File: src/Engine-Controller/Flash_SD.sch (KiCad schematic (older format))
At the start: 5 parts, among them P6 Micro_SD_Card, U5 SST25VF040B-50-4I-S2AE-T

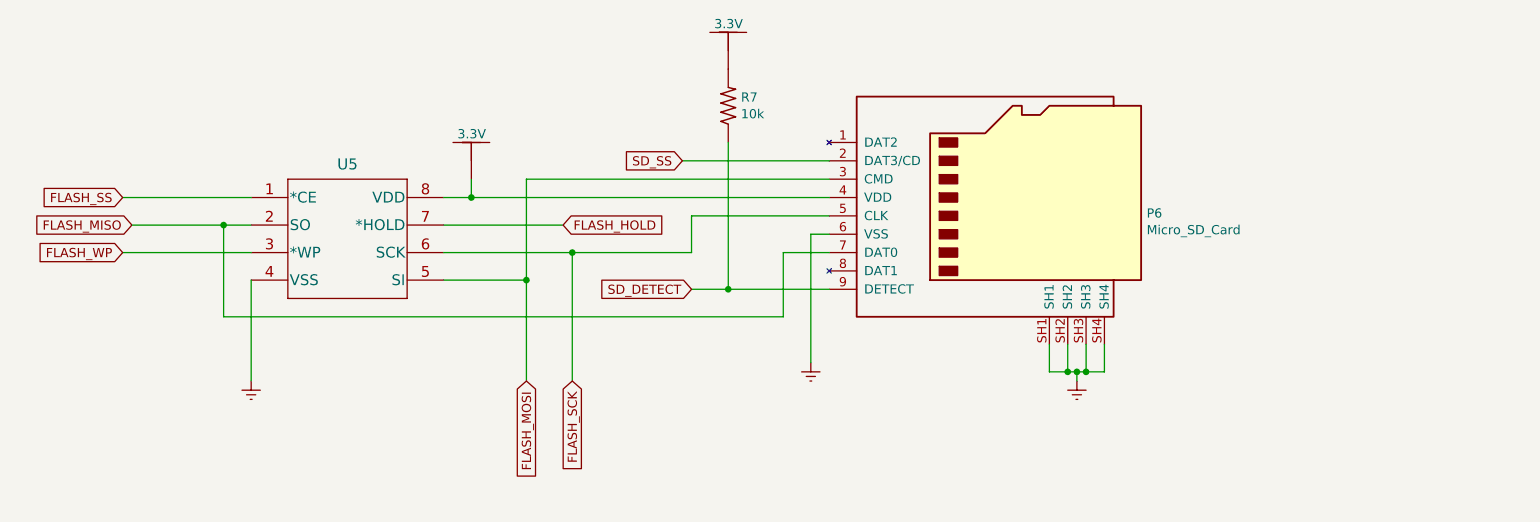
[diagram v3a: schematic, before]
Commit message: Added ADC Inputs
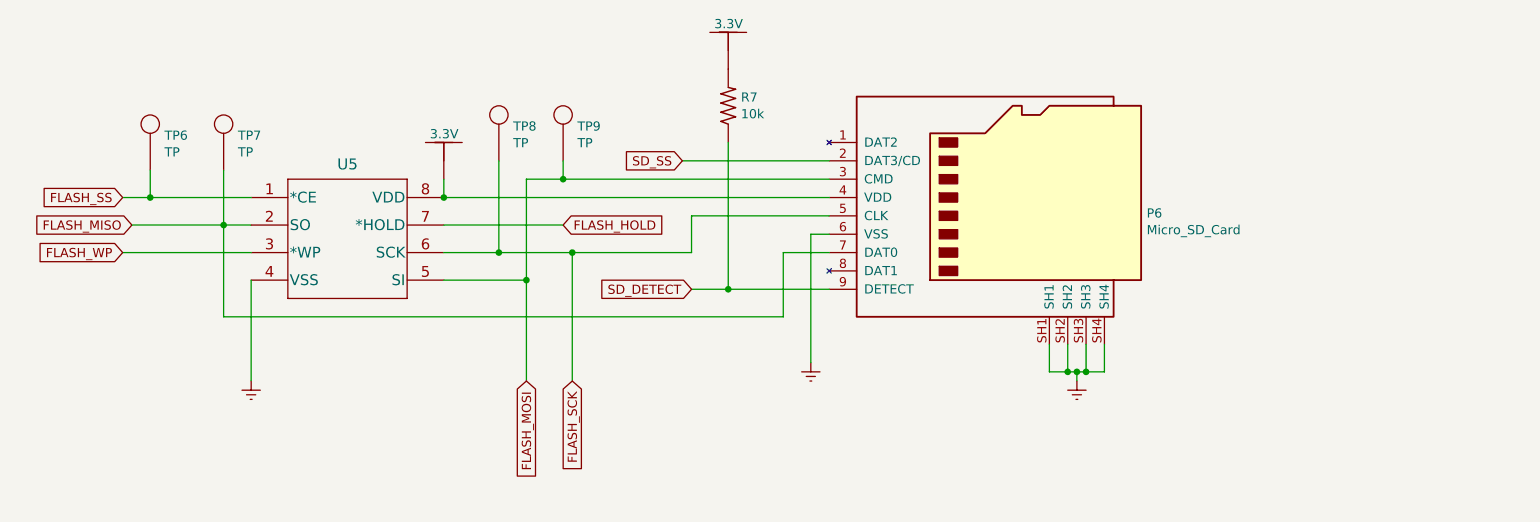
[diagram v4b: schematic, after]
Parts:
- added TP6, TP7, TP8, TP9: TP, symbol Engine-Controller:TP
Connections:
- net FLASH_MISO: now also TP7.1
- net FLASH_MOSI: now also TP9.1
- net FLASH_SCK: now also TP8.1
- net FLASH_SS: now also TP6.1
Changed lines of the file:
@@
 $Descr A4 11693 8268
 encoding utf-8
-Sheet 6 5
+Sheet 5 5
 Title "Data Logging Memory"
 Date "2021-07-03"
@@
 FLASH_SS
 Wire Wire Line
-	3300 3800 4000 3800
+	3300 3800 3450 3800
 Text GLabel 3350 3950 0    50   Input ~ 0
 FLASH_MISO
@@
 L Engine-Controller:3.3V None05
 U 1 1 617870C5
-P 5200 3550
-F 0 "None05" H 5328 3539 50  0001 L CNN
-F 1 "3.3V" H 5124 3646 50  0000 L CNN
-F 2 "" H 5200 3550 50  0001 C CNN
-F 3 "" H 5200 3550 50  0001 C CNN
-	1    5200 3550
-	1    0    0    -1
-$EndComp
-Wire Wire Line
-	5050 3800 5200 3800
-Wire Wire Line
-	5200 3800 5200 3700
+P 5050 3550
+F 0 "None05" H 5178 3539 50  0001 L CNN
+F 1 "3.3V" H 4974 3646 50  0000 L CNN
+F 2 "" H 5050 3550 50  0001 C CNN
+F 3 "" H 5050 3550 50  0001 C CNN
+	1    5050 3550
+	1    0    0    -1
+$EndComp
+Wire Wire Line
+	5050 3800 5050 3700
 $Comp
 L power:Earth #PWR03
@@
 FLASH_SCK
 Wire Wire Line
-	5750 4100 5050 4100
+	5750 4100 5350 4100
 Text GLabel 5500 4800 3    50   Input ~ 0
 FLASH_MOSI
@@
 	8650 4750 8550 4750
 Connection ~ 8550 4750
-Wire Wire Line
-	5200 3800 7150 3800
-Connection ~ 5200 3800
 Text GLabel 6350 3600 0    50   Input ~ 0
 SD_SS
@@
 	5500 4250 5500 3700
 Wire Wire Line
-	5500 3700 7150 3700
+	5500 3700 5700 3700
 Connection ~ 5500 4250
 Wire Wire Line
@@
 	1    0    0    -1
 $EndComp
+$Comp
+L Engine-Controller:TP TP6
+U 1 1 619D48B0
+P 3450 3650
+F 0 "TP6" H 3528 3838 50  0000 L CNN
+F 1 "TP" H 3528 3747 50  0000 L CNN
+F 2 "" H 3450 3650 50  0001 C CNN
+F 3 "" H 3450 3650 50  0001 C CNN
+	1    3450 3650
+	1    0    0    -1
+$EndComp
+$Comp
+L Engine-Controller:TP TP7
+U 1 1 619D6A4E
+P 3850 3650
+F 0 "TP7" H 3928 3838 50  0000 L CNN
+F 1 "TP" H 3928 3747 50  0000 L CNN
+F 2 "" H 3850 3650 50  0001 C CNN
+F 3 "" H 3850 3650 50  0001 C CNN
+	1    3850 3650
+	1    0    0    -1
+$EndComp
+$Comp
+L Engine-Controller:TP TP8
+U 1 1 619D874E
+P 5350 3600
+F 0 "TP8" H 5428 3788 50  0000 L CNN
+F 1 "TP" H 5428 3697 50  0000 L CNN
+F 2 "" H 5350 3600 50  0001 C CNN
+F 3 "" H 5350 3600 50  0001 C CNN
+	1    5350 3600
+	1    0    0    -1
+$EndComp
+Connection ~ 5050 3800
+Wire Wire Line
+	5050 3800 7150 3800
+$Comp
+L Engine-Controller:TP TP9
+U 1 1 619DE8D4
+P 5700 3600
+F 0 "TP9" H 5778 3788 50  0000 L CNN
+F 1 "TP" H 5778 3697 50  0000 L CNN
+F 2 "" H 5700 3600 50  0001 C CNN
+F 3 "" H 5700 3600 50  0001 C CNN
+	1    5700 3600
+	1    0    0    -1
+$EndComp
+Wire Wire Line
+	3450 3650 3450 3800
+Connection ~ 3450 3800
+Wire Wire Line
+	3450 3800 4000 3800
+Wire Wire Line
+	3850 3650 3850 3950
+Wire Wire Line
+	5350 3600 5350 4100
+Connection ~ 5350 4100
+Wire Wire Line
+	5350 4100 5050 4100
+Wire Wire Line
+	5700 3600 5700 3700
+Connection ~ 5700 3700
+Wire Wire Line
+	5700 3700 7150 3700
 $EndSCHEMATC

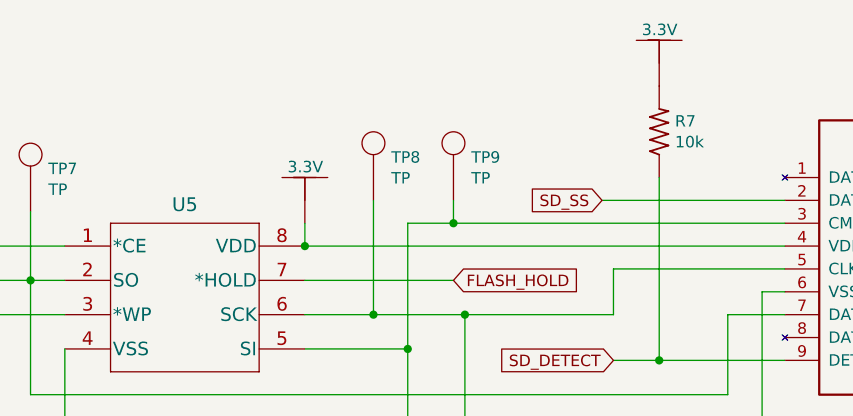
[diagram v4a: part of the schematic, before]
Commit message: Fixed Schematic ERC erros
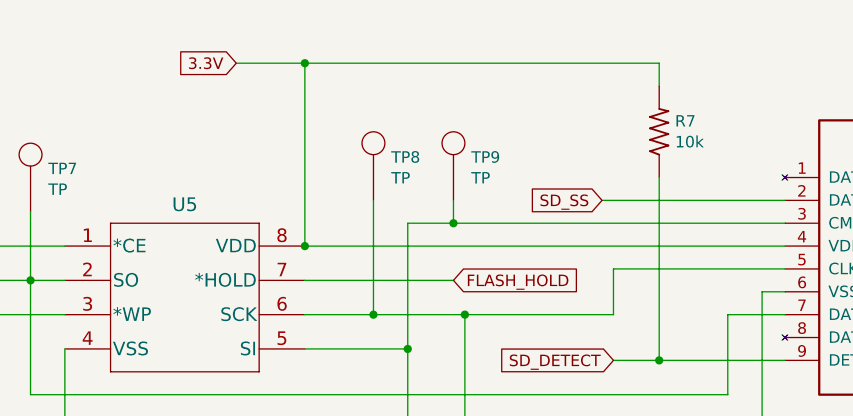
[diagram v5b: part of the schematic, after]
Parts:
- removed None05, None06: 3.3V, symbol Engine-Controller:3.3V
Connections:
- net 3.3V: now reaches P6.4 (VDD), U5.8 (VDD)
- net 3.3V: now also R7.2
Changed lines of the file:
@@
 	4000 4100 3300 4100
-$Comp
-L Engine-Controller:3.3V None05
-U 1 1 617870C5
-P 5050 3550
-F 0 "None05" H 5178 3539 50  0001 L CNN
-F 1 "3.3V" H 4974 3646 50  0000 L CNN
-F 2 "" H 5050 3550 50  0001 C CNN
-F 3 "" H 5050 3550 50  0001 C CNN
-	1    5050 3550
-	1    0    0    -1
-$EndComp
-Wire Wire Line
-	5050 3800 5050 3700
 $Comp
 L power:Earth #PWR03
@@
 	6600 4300 6400 4300
 $Comp
-L Engine-Controller:3.3V None06
-U 1 1 618DC655
-P 6600 2950
-F 0 "None06" H 6728 2939 50  0001 L CNN
-F 1 "3.3V" H 6524 3046 50  0000 L CNN
-F 2 "" H 6600 2950 50  0001 C CNN
-F 3 "" H 6600 2950 50  0001 C CNN
-	1    6600 2950
-	1    0    0    -1
-$EndComp
-$Comp
 L Engine-Controller:TP TP6
 U 1 1 619D48B0
@@
 Wire Wire Line
 	5700 3700 7150 3700
+Text GLabel 4750 3000 0    50   Input ~ 0
+3.3V
+Wire Wire Line
+	4750 3000 5050 3000
+Wire Wire Line
+	6600 3000 6600 3100
+Wire Wire Line
+	5050 3000 5050 3800
+Connection ~ 5050 3000
+Wire Wire Line
+	5050 3000 6600 3000
 $EndSCHEMATC

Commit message: Routed decoupling caps
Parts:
- P6: footprint (none) -> Engine-Controller:GCT_MEM2075-00-140-01-A
- R7: footprint (none) -> Engine-Controller:RES_0603
- TP6, TP7, TP8, TP9: footprint (none) -> Engine-Controller:TP
- U5: footprint SOIC8_S2A_SST_MCH -> Engine-Controller:SST25VF040B-50-4I-S2AE-T
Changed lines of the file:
@@
 F 0 "U5" H 4525 4181 60  0000 C CNN
 F 1 "SST25VF040B-50-4I-S2AE-T" H 4525 4181 60  0001 C CNN
-F 2 "SOIC8_S2A_SST_MCH" H 4550 3200 60  0001 C CNN
+F 2 "Engine-Controller:SST25VF040B-50-4I-S2AE-T" H 4550 3200 60  0001 C CNN
 F 3 "" H 3350 3950 60  0001 C CNN
 	1    4550 3900
@@
 F 0 "P6" H 8880 3714 50  0000 L CNN
 F 1 "Micro_SD_Card" H 8880 3623 50  0000 L CNN
-F 2 "" H 9200 4100 50  0001 C CNN
+F 2 "Engine-Controller:GCT_MEM2075-00-140-01-A" H 9200 4100 50  0001 C CNN
 F 3 "http://katalog.we-online.de/em/datasheet/693072010801.pdf" H 8050 3800 50  0001 C CNN
 	1    8050 3800
@@
 F 0 "R7" V 6646 3231 50  0000 R CNN
 F 1 "10k" V 6555 3231 50  0000 R CNN
-F 2 "" H 6650 2800 50  0001 L BNN
+F 2 "Engine-Controller:RES_0603" H 6650 2800 50  0001 L BNN
 F 3 "" H 6600 3300 50  0001 L BNN
 	1    6600 3300
@@
 F 0 "TP6" H 3528 3838 50  0000 L CNN
 F 1 "TP" H 3528 3747 50  0000 L CNN
-F 2 "" H 3450 3650 50  0001 C CNN
+F 2 "Engine-Controller:TP" H 3450 3650 50  0001 C CNN
 F 3 "" H 3450 3650 50  0001 C CNN
 	1    3450 3650
@@
 F 0 "TP7" H 3928 3838 50  0000 L CNN
 F 1 "TP" H 3928 3747 50  0000 L CNN
-F 2 "" H 3850 3650 50  0001 C CNN
+F 2 "Engine-Controller:TP" H 3850 3650 50  0001 C CNN
 F 3 "" H 3850 3650 50  0001 C CNN
 	1    3850 3650
@@
 F 0 "TP8" H 5428 3788 50  0000 L CNN
 F 1 "TP" H 5428 3697 50  0000 L CNN
-F 2 "" H 5350 3600 50  0001 C CNN
+F 2 "Engine-Controller:TP" H 5350 3600 50  0001 C CNN
 F 3 "" H 5350 3600 50  0001 C CNN
 	1    5350 3600
@@
 F 0 "TP9" H 5778 3788 50  0000 L CNN
 F 1 "TP" H 5778 3697 50  0000 L CNN
-F 2 "" H 5700 3600 50  0001 C CNN
+F 2 "Engine-Controller:TP" H 5700 3600 50  0001 C CNN
 F 3 "" H 5700 3600 50  0001 C CNN
 	1    5700 3600
